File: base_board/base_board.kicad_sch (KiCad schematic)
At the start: 62 parts, among them J1 Conn_ARM_JTAG_SWD_20, J3 Conn_01x04, SW1 SW_Push, U1 STM32F446ZEJx, U2 IS42S16400J-xT, U3 BMI270, U4 USB_C_Receptacle_USB2.0, U5 10p, U6 10p, U7 LD3985M33R_SOT23, Y1 Crystal_GND24

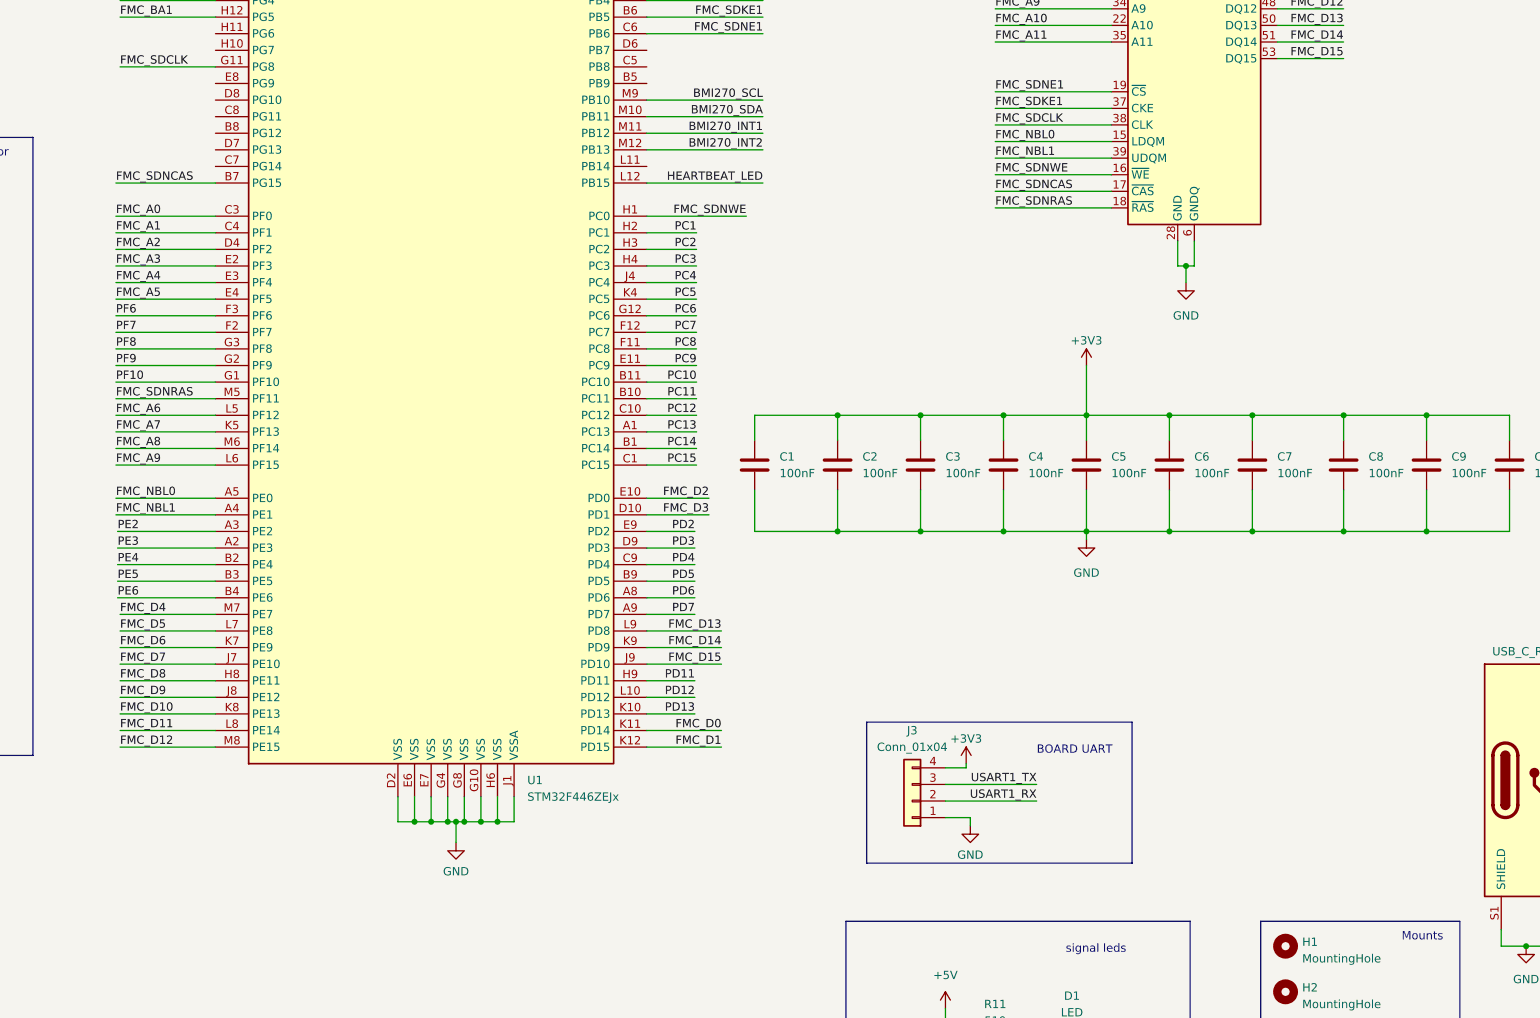
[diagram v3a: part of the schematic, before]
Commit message: [pcb][schematic] added SPI header for the board(#4)
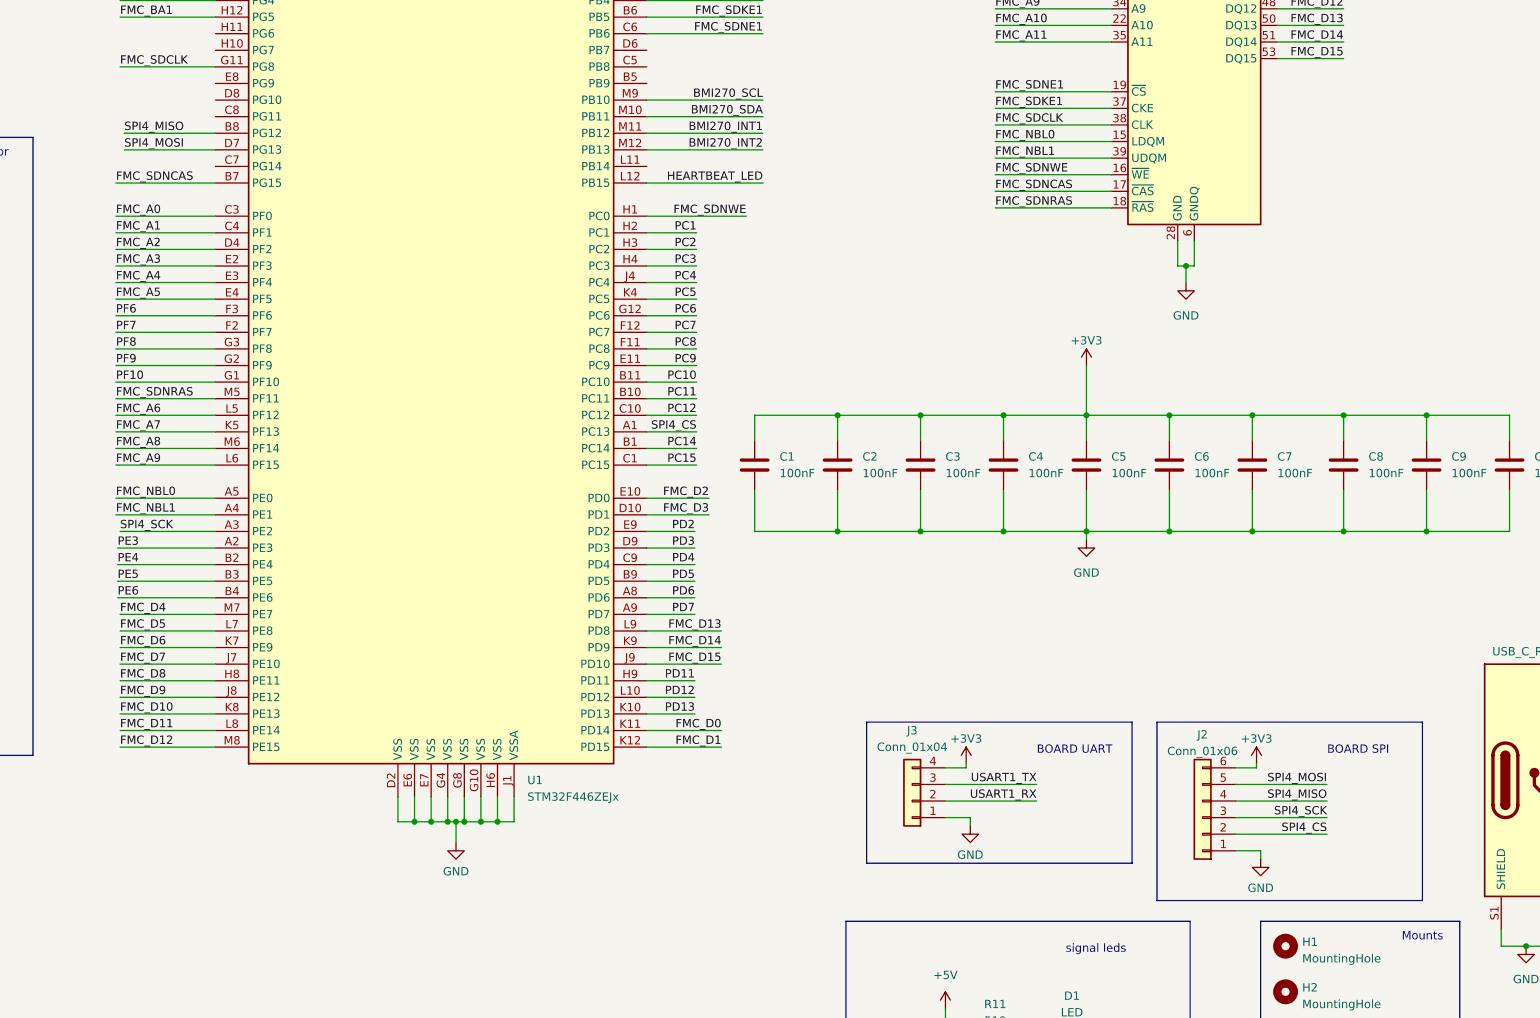
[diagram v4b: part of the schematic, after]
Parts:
- added J2: Conn_01x06, Connector_PinHeader_2.54mm:PinHeader_1x06_P2.54mm_Vertical, symbol Connector_Generic:Conn_01x06
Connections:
- net +3V3: now also J2.6 (Pin_6)
- net GND: now also J2.1 (Pin_1)
- net SPI4_MISO: now reaches U1.B8 (PG12)
- net SPI4_MISO: now also J2.4 (Pin_4)
- net SPI4_MOSI: now reaches U1.D7 (PG13)
- net SPI4_MOSI: now also J2.5 (Pin_5)
- net PC13 renamed SPI4_CS
- net SPI4_CS: now also J2.2 (Pin_2)
- net PE2 renamed SPI4_SCK
- net SPI4_SCK: now also J2.3 (Pin_3)
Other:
- note added: "BOARD SPI"
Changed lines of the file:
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@@
     (stroke (width 0) (type default))
   )
-  (wire (pts (xy 123.444 165.1) (xy 138.43 165.1))
+  (wire (pts (xy 297.815 201.295) (xy 294.64 201.295))
     (stroke (width 0) (type default))
   )
@@
     (stroke (width 0) (type default))
   )
+  (wire (pts (xy 294.64 208.915) (xy 308.61 208.915))
+    (stroke (width 0) (type default))
+  )
   (wire (pts (xy 365.125 182.245) (xy 361.95 182.245))
     (stroke (width 0) (type default))
@@
     (stroke (width 0) (type default))
   )
+  (wire (pts (xy 138.43 106.68) (xy 124.46 106.68))
+    (stroke (width 0) (type default))
+  )
   (wire (pts (xy 45.72 257.81) (xy 39.37 257.81))
     (stroke (width 0) (type default))
@@
     (stroke (width 0) (type default))
   )
+  (wire (pts (xy 297.815 200.66) (xy 297.815 201.295))
+    (stroke (width 0) (type default))
+  )
   (wire (pts (xy 161.29 22.86) (xy 161.29 19.685))
     (stroke (width 0) (type default))
@@
     (stroke (width 0) (type default))
   )
+  (wire (pts (xy 298.45 215.265) (xy 298.45 213.995))
+    (stroke (width 0) (type default))
+  )
   (wire (pts (xy 271.78 243.84) (xy 278.765 243.84))
     (stroke (width 0) (type default))
@@
     (stroke (width 0) (type default))
   )
+  (wire (pts (xy 294.64 211.455) (xy 308.61 211.455))
+    (stroke (width 0) (type default))
+  )
   (wire (pts (xy 176.53 205.74) (xy 176.53 209.55))
     (stroke (width 0) (type default))
@@
     (stroke (width 0) (type default))
   )
+  (wire (pts (xy 298.45 213.995) (xy 294.64 213.995))
+    (stroke (width 0) (type default))
+  )
   (wire (pts (xy 171.45 19.685) (xy 168.91 19.685))
     (stroke (width 0) (type default))
@@
     (stroke (width 0) (type default))
   )
+  (wire (pts (xy 123.825 165.1) (xy 138.43 165.1))
+    (stroke (width 0) (type default))
+  )
   (wire (pts (xy 284.48 151.13) (xy 284.48 147.32))
     (stroke (width 0) (type default))
@@
     (stroke (width 0) (type default))
   )
+  (wire (pts (xy 294.64 206.375) (xy 308.61 206.375))
+    (stroke (width 0) (type default))
+  )
   (wire (pts (xy 257.81 100.33) (xy 275.59 100.33))
     (stroke (width 0) (type default))
@@
     (stroke (width 0) (type default))
   )
+  (wire (pts (xy 294.64 203.835) (xy 308.61 203.835))
+    (stroke (width 0) (type default))
+  )
   (wire (pts (xy 204.47 167.64) (xy 211.836 167.64))
     (stroke (width 0) (type default))
@@
     (stroke (width 0) (type default))
   )
+  (wire (pts (xy 138.43 104.14) (xy 124.46 104.14))
+    (stroke (width 0) (type default))
+  )
   (wire (pts (xy 204.47 38.1) (xy 211.328 38.1))
     (stroke (width 0) (type default))
@@
     (fill (type none))
   )
+  (rectangle (start 282.575 194.31) (end 323.215 221.615)
+    (stroke (width 0) (type default))
+    (fill (type none))
+  )
+  (text "BOARD SPI\n" (at 308.61 199.39 0)
+    (effects (font (size 1.27 1.27)) (justify left bottom))
+  )
   (text "JTAG" (at 86.995 17.78 0)
     (effects (font (size 1.27 1.27)) (justify left bottom))
@@
     (effects (font (size 1.27 1.27)) (justify right bottom))
   )
+  (label "SPI4_CS" (at 212.09 149.86 180) (fields_autoplaced)
+    (effects (font (size 1.27 1.27)) (justify right bottom))
+  )
   (label "FMC_A8" (at 257.81 82.55 0) (fields_autoplaced)
     (effects (font (size 1.27 1.27)) (justify left bottom))
@@
     (effects (font (size 1.27 1.27)) (justify right bottom))
   )
+  (label "SPI4_MOSI" (at 124.46 106.68 0) (fields_autoplaced)
+    (effects (font (size 1.27 1.27)) (justify left bottom))
+  )
   (label "PF10" (at 123.19 142.24 0) (fields_autoplaced)
     (effects (font (size 1.27 1.27)) (justify left bottom))
@@
     (effects (font (size 1.27 1.27)) (justify right bottom))
   )
+  (label "SPI4_MISO" (at 124.46 104.14 0) (fields_autoplaced)
+    (effects (font (size 1.27 1.27)) (justify left bottom))
+  )
   (label "FMC_A2" (at 123.19 121.92 0) (fields_autoplaced)
     (effects (font (size 1.27 1.27)) (justify left bottom))
@@
     (effects (font (size 1.27 1.27)) (justify left bottom))
   )
+  (label "SPI4_SCK" (at 123.825 165.1 0) (fields_autoplaced)
+    (effects (font (size 1.27 1.27)) (justify left bottom))
+  )
   (label "FMC_D0" (at 215.9 195.58 180) (fields_autoplaced)
     (effects (font (size 1.27 1.27)) (justify right bottom))
@@
     (effects (font (size 1.27 1.27)) (justify left bottom))
   )
+  (label "SPI4_MISO" (at 308.61 206.375 180) (fields_autoplaced)
+    (effects (font (size 1.27 1.27)) (justify right bottom))
+  )
+  (label "SPI4_MOSI" (at 308.61 203.835 180) (fields_autoplaced)
+    (effects (font (size 1.27 1.27)) (justify right bottom))
+  )
   (label "HEARTBEAT_LED" (at 222.25 111.76 180) (fields_autoplaced)
     (effects (font (size 1.27 1.27)) (justify right bottom))
@@
     (effects (font (size 1.27 1.27)) (justify right bottom))
   )
+  (label "SPI4_CS" (at 308.61 211.455 180) (fields_autoplaced)
+    (effects (font (size 1.27 1.27)) (justify right bottom))
+  )
   (label "FMC_D12" (at 123.825 198.12 0) (fields_autoplaced)
     (effects (font (size 1.27 1.27)) (justify left bottom))
@@
     (effects (font (size 1.27 1.27)) (justify left bottom))
   )
-  (label "PE2" (at 123.444 165.1 0) (fields_autoplaced)
-    (effects (font (size 1.27 1.27)) (justify left bottom))
-  )
   (label "PC15" (at 212.09 154.94 180) (fields_autoplaced)
     (effects (font (size 1.27 1.27)) (justify right bottom))
@@
     (effects (font (size 1.27 1.27)) (justify right bottom))
   )
+  (label "SPI4_SCK" (at 308.61 208.915 180) (fields_autoplaced)
+    (effects (font (size 1.27 1.27)) (justify right bottom))
+  )
   (label "PA8" (at 211.836 50.8 180) (fields_autoplaced)
     (effects (font (size 1.27 1.27)) (justify right bottom))
   )
   (label "PD5" (at 211.836 172.72 180) (fields_autoplaced)
-    (effects (font (size 1.27 1.27)) (justify right bottom))
-  )
-  (label "PC13" (at 212.09 149.86 180) (fields_autoplaced)
     (effects (font (size 1.27 1.27)) (justify right bottom))
   )
@@
     )
   )
+  (symbol (lib_name "GND_2") (lib_id "power:GND") (at 298.45 215.265 0) (unit 1)
+    (in_bom yes) (on_board yes) (dnp no) (fields_autoplaced)
+    (property "Reference" "#PWR015" (at 298.45 221.615 0)
+      (effects (font (size 1.27 1.27)) hide)
+    )
+    (property "Value" "GND" (at 298.45 219.71 0)
+      (effects (font (size 1.27 1.27)))
+    )
+    (property "Footprint" "" (at 298.45 215.265 0)
+      (effects (font (size 1.27 1.27)) hide)
+    )
+    (property "Datasheet" "" (at 298.45 215.265 0)
+      (effects (font (size 1.27 1.27)) hide)
+    )
+    (pin "1")
+    (instances
+      (project "base_board"
+        (path "/2307506f-1d7e-4fdb-b101-b9905788fe29"
+          (reference "#PWR015") (unit 1)
+        )
+      )
+    )
+  )
   (symbol (lib_id "Connector:TestPoint") (at 39.37 140.97 90) (unit 1)
     (in_bom yes) (on_board yes) (dnp no) (fields_autoplaced)
@@
         (path "/2307506f-1d7e-4fdb-b101-b9905788fe29"
           (reference "TP2") (unit 1)
+        )
+      )
+    )
+  )
+  (symbol (lib_name "+3V3_8") (lib_id "power:+3V3") (at 297.815 200.66 0) (unit 1)
+    (in_bom yes) (on_board yes) (dnp no) (fields_autoplaced)
+    (property "Reference" "#PWR014" (at 297.815 204.47 0)
+      (effects (font (size 1.27 1.27)) hide)
+    )
+    (property "Value" "+3V3" (at 297.815 196.85 0)
+      (effects (font (size 1.27 1.27)))
+    )
+    (property "Footprint" "" (at 297.815 200.66 0)
+      (effects (font (size 1.27 1.27)) hide)
+    )
+    (property "Datasheet" "" (at 297.815 200.66 0)
+      (effects (font (size 1.27 1.27)) hide)
+    )
+    (pin "1")
+    (instances
+      (project "base_board"
+        (path "/2307506f-1d7e-4fdb-b101-b9905788fe29"
+          (reference "#PWR014") (unit 1)
         )
       )
@@
         )
       )
+    )
+  )
+  (symbol (lib_id "Connector_Generic:Conn_01x06") (at 289.56 208.915 180) (unit 1)
+    (in_bom yes) (on_board yes) (dnp no) (fields_autoplaced)
+    (property "Reference" "J2" (at 289.56 196.215 0)
+      (effects (font (size 1.27 1.27)))
+    )
+    (property "Value" "Conn_01x06" (at 289.56 198.755 0)
+      (effects (font (size 1.27 1.27)))
+    )
+    (property "Footprint" "Connector_PinHeader_2.54mm:PinHeader_1x06_P2.54mm_Vertical" (at 289.56 208.915 0)
+      (effects (font (size 1.27 1.27)) hide)
+    )
+    (property "Datasheet" "~" (at 289.56 208.915 0)
+      (effects (font (size 1.27 1.27)) hide)
+    )
+    (pin "1")
+    (pin "2")
+    (pin "3")
+    (pin "4")
+    (pin "5")
+    (pin "6")
+    (instances
+      (project "base_board"
+        (path "/2307506f-1d7e-4fdb-b101-b9905788fe29"
+          (reference "J2") (unit 1)
+        )
+      )

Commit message: Moved sensor to hierarchical sheet
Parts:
- removed C10, C11: 100nF, Capacitor_SMD:C_0603_1608Metric, symbol Device:C
- removed JP3: SolderJumper_3_Open, Jumper:SolderJumper-3_P1.3mm_Open_RoundedPad1.0x1.5mm, symbol Jumper:SolderJumper_3_Open
- removed R8, R9: 4.7K, Resistor_SMD:R_0603_1608Metric, symbol Device:R
- removed TP1, TP2: TestPoint, TestPoint:TestPoint_Pad_D3.0mm, symbol Connector:TestPoint
- removed U3: BMI270, BMI270:XDCR_BMI270, symbol BMI270:BMI270
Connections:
- no-connect marks 6 -> 3
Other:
- added sheet sensors (sensors.kicad_sch)
- note removed: "imu sensor"
